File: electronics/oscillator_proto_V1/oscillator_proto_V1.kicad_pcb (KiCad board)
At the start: 2 copper layers, 42.5 x 46.2 mm, 27 parts, among them J1 module_2x15_left_input, J2 module_2x15_right_input, J3 Coax, U1 TL081, U2 LME49720, U3 TL082

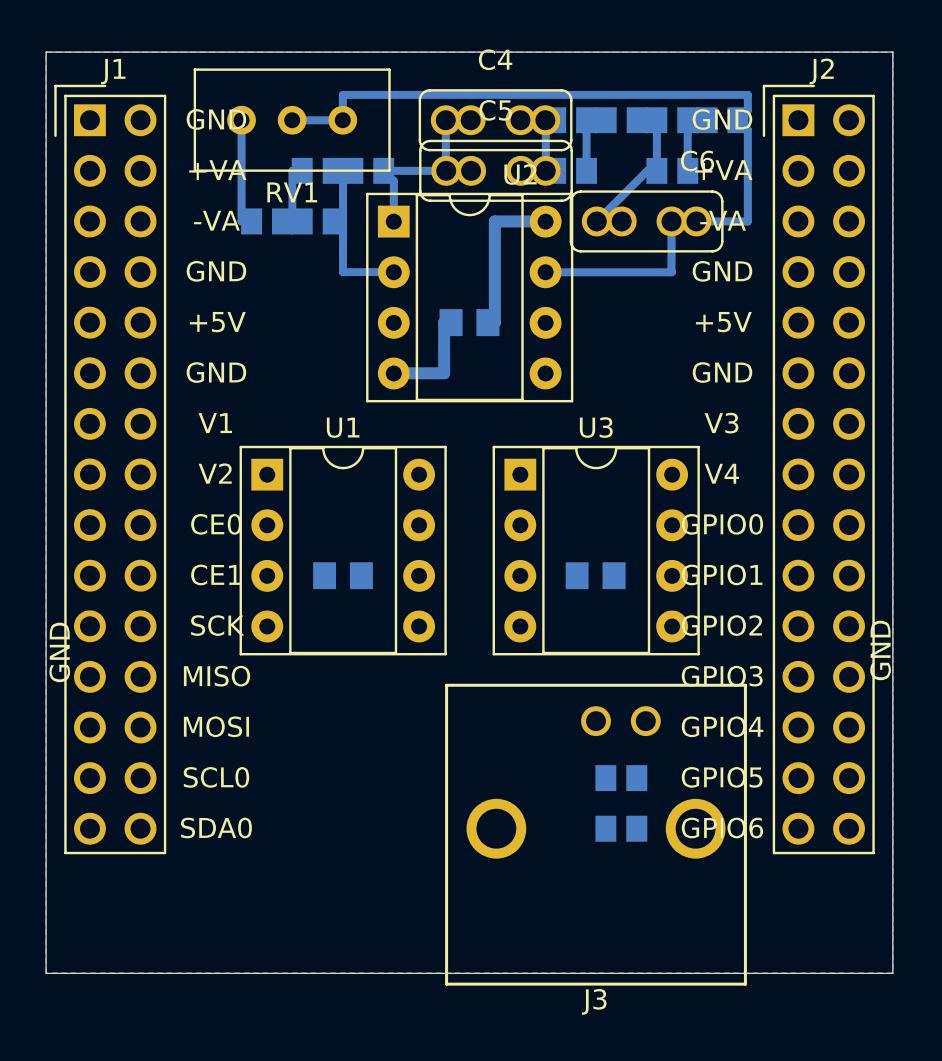
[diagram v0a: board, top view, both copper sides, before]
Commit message: layout completed on prototype oscillator prototype
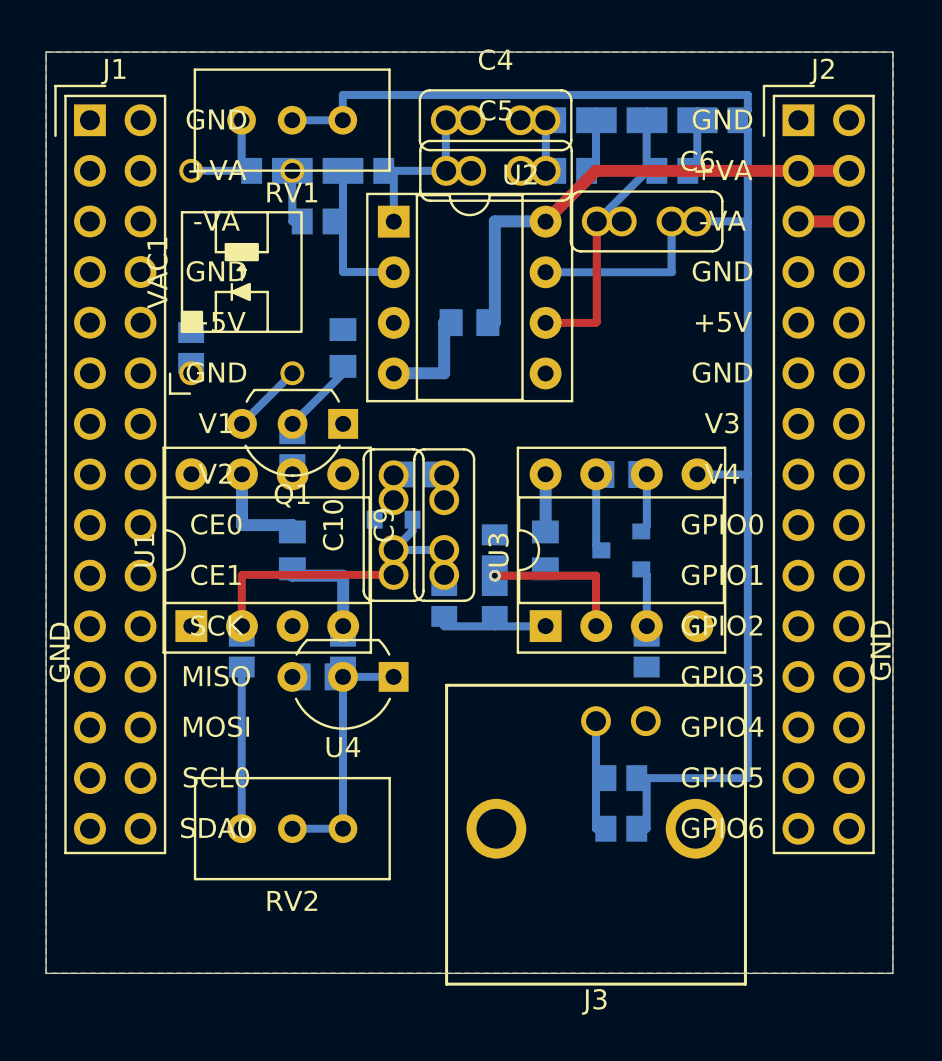
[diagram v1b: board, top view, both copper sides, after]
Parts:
- added C10: 100n, SquantorRcl:C-025_050-030X100-film, F.Cu at (160.0, 92.7)
- added C11: 10u, SquantorRcl:C_0805+0603, B.Cu at (157.5, 83.8)
- added C7: 47p, SquantorRcl:C_0805+0603, B.Cu at (171.4, 90.2)
- added C8: 10u, SquantorRcl:C_0805+0603, B.Cu at (156.2, 100.3)
- added C9: 47u, SquantorRcl:C-025_050-030X100-film, F.Cu at (162.6, 92.7)
- added D1: BAV99, SquantorIC:SOT23-3, B.Cu at (171.4, 94.0)
- added D2: BAV99, SquantorIC:SOT23-3, B.Cu at (160.0, 91.4)
- added Q1: BC337, Package_TO_SOT_THT:TO-92L_Inline_Wide, F.Cu at (157.5, 87.6)
- added R13: 510, SquantorRcl:R_0805+0603, B.Cu at (149.9, 83.8)
- added R14: 10K, SquantorRcl:R_0805+0603, B.Cu at (165.1, 96.5)
- added R15: 10K, SquantorRcl:R_0805+0603, B.Cu at (165.1, 94.0)
- added R16: 10K, SquantorRcl:R_0805+0603, B.Cu at (172.7, 99.1)
- added R17: 8K2, SquantorRcl:R_0805+0603, B.Cu at (157.5, 99.1)
- added R18: 27K, SquantorRcl:R_0805+0603, B.Cu at (162.6, 96.5)
- added R19: 8K2, SquantorRcl:R_0805+0603, B.Cu at (152.4, 99.1)
- added R20: 8K2, SquantorRcl:R_0805+0603, B.Cu at (161.3, 90.2)
- added R21: 2K2, SquantorRcl:R_0805+0603, B.Cu at (154.9, 88.9)
- added RV2: 50K, Potentiometer_THT:Potentiometer_Bourns_3296W_Vertical, F.Cu at (152.4, 108.0)
- added U4: TL431, Package_TO_SOT_THT:TO-92_Inline_Wide, F.Cu at (160.0, 100.3)
- added VAC1: NSL32R3, SquantorOpto:NSL32SR3, F.Cu at (152.4, 80.0)
- moved N1 8.98 mm to (165.7, 105.5)
- moved N2 8.98 mm to (165.1, 101.6)
- moved U1 8.50 mm to (149.9, 97.8), turned to 90 degrees
- moved U3 7.71 mm to (167.7, 97.8), turned to 90 degrees
- moved C1 2.84 mm to (154.9, 94.0), turned to 90 degrees
- moved C3 2.82 mm to (167.6, 94.0), turned to 90 degrees
- moved R9 2.54 mm to (153.7, 74.9)
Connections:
- U1 pad 2: unconnected-(U1-Pad2) -> Net-(U1-Pad2)
- U1 pad 3: unconnected-(U1-Pad3) -> GND
- U1 pad 6: unconnected-(U1-Pad6) -> Net-(U1-Pad6)
- U3 pad 1: unconnected-(U3-Pad1) -> /GAIN_INPUT
- U3 pad 2: unconnected-(U3-Pad2) -> Net-(U3-Pad2)
- U3 pad 3: unconnected-(U3-Pad3) -> Net-(R16-Pad2)
- U3 pad 5: unconnected-(U3-Pad5) -> /OUTPUT
- U3 pad 6: unconnected-(U3-Pad6) -> Net-(U3-Pad6)
- U3 pad 7: unconnected-(U3-Pad7) -> Net-(U3-Pad7)
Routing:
- net /OUTPUT: track 42.4 -> 81.5 mm
- net +15V: track 7.98 -> 32.6 mm
- net Net-(U1-Pad2): track 0.00 -> 14.6 mm
- net Net-(C8-Pad2): track 0.00 -> 12.7 mm
- net Net-(U2-Pad6): track 7.60 -> 16.0 mm
- net Net-(R19-Pad2): track 0.00 -> 8.12 mm
- net -15V: track 5.42 -> 13.4 mm
- net Net-(U3-Pad2): track 0.00 -> 7.61 mm, vias 0 -> 1
- net Net-(J3-Pad1): track 0.00 -> 6.39 mm
- net /GAIN_INPUT: track 0.00 -> 6.08 mm
- net Net-(C11-Pad2): track 0.00 -> 3.93 mm
- net Net-(U3-Pad7): track 0.00 -> 3.93 mm
- net /GAIN: track 0.00 -> 3.59 mm
- net Net-(U3-Pad6): track 0.00 -> 2.99 mm
- net Net-(R16-Pad2): track 0.00 -> 2.97 mm
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
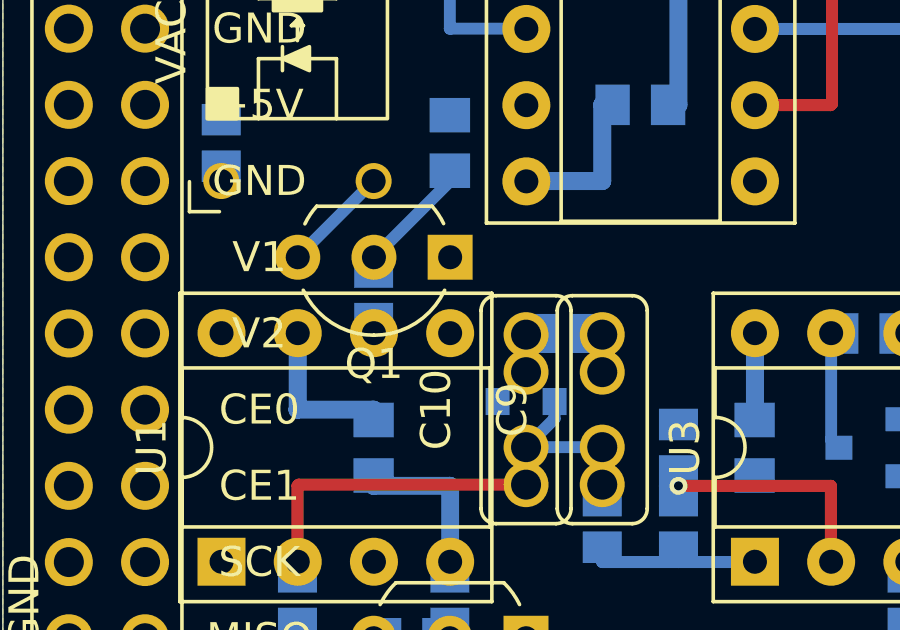
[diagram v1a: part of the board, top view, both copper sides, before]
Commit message: updated resistor values and some minor routing updates
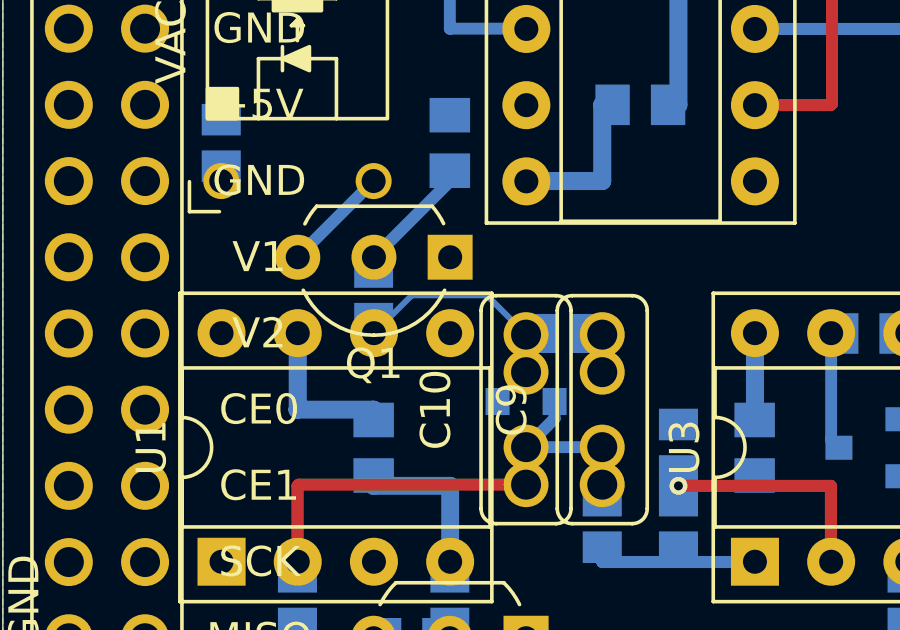
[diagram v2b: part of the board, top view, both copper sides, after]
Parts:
- N1: value 20220421 -> 20220423
- R11, R12: value 3k6 -> 3k
- R9: value 18 -> 15
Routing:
- net Net-(C10-Pad2): track 0.00 -> 6.13 mm

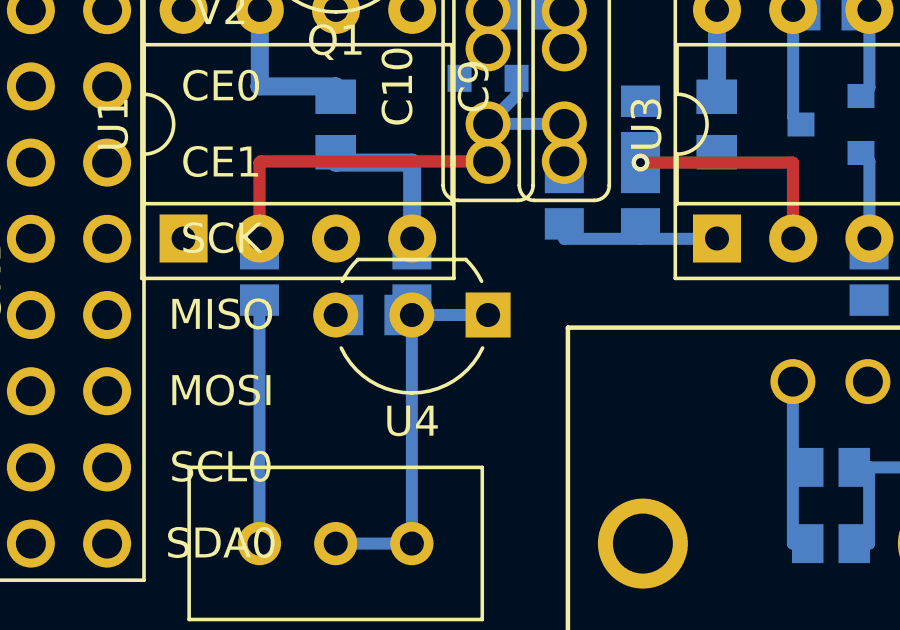
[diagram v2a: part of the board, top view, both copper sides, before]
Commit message: fixed errors with proto oscillator
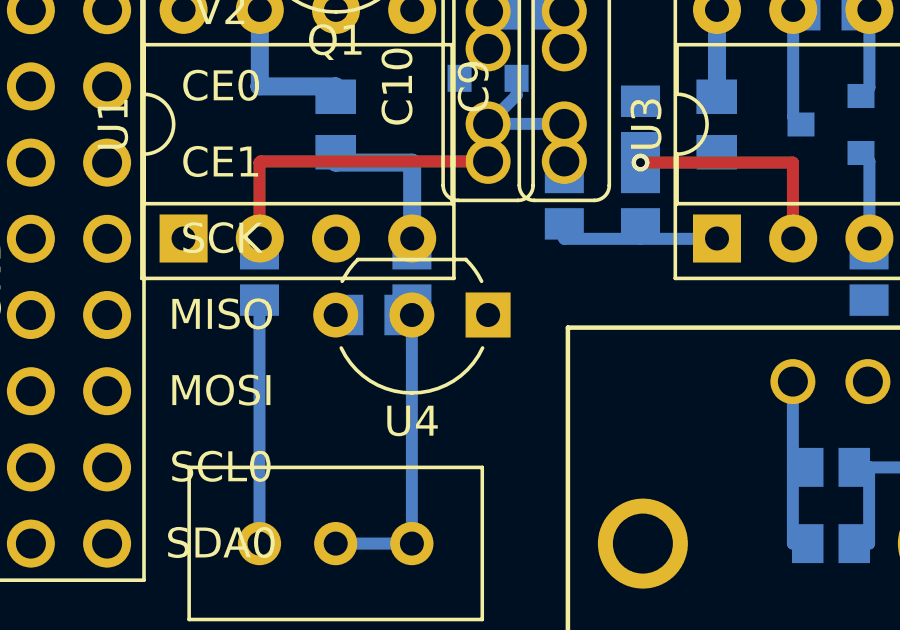
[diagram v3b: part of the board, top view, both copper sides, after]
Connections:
- U4 pad 1: Net-(C8-Pad2) -> GND
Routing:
- net Net-(C8-Pad2): track 12.7 -> 10.2 mm
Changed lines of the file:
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@@
     (fp_arc (start 0.786375 1.753625) (mid 0.248779 -0.949055) (end 2.54 -2.48) (layer "F.Fab") (width 0.1))
     (pad "1" thru_hole rect (at 0 0 180) (size 1.5 1.5) (drill 0.8) (layers *.Cu *.Mask)
-      (net 43 "Net-(C8-Pad2)") (pinfunction "REF") (pintype "passive"))
+      (net 1 "GND") (pinfunction "REF") (pintype "passive"))
     (pad "2" thru_hole circle (at 2.54 0 180) (size 1.5 1.5) (drill 0.8) (layers *.Cu *.Mask)
       (net 43 "Net-(C8-Pad2)") (pinfunction "A") (pintype "passive"))
@@
   (segment (start 152.41 87.62) (end 154.94 85.09) (width 0.4) (layer "B.Cu") (net 42))
   (segment (start 157.48 107.95) (end 157.48 100.33) (width 0.4) (layer "B.Cu") (net 43))
-  (segment (start 157.48 100.33) (end 160.02 100.33) (width 0.4) (layer "B.Cu") (net 43))
   (segment (start 154.94 107.95) (end 157.48 107.95) (width 0.4) (layer "B.Cu") (net 43))
   (segment (start 158.71 88.9) (end 156.21 88.9) (width 0.2) (layer "B.Cu") (net 44))

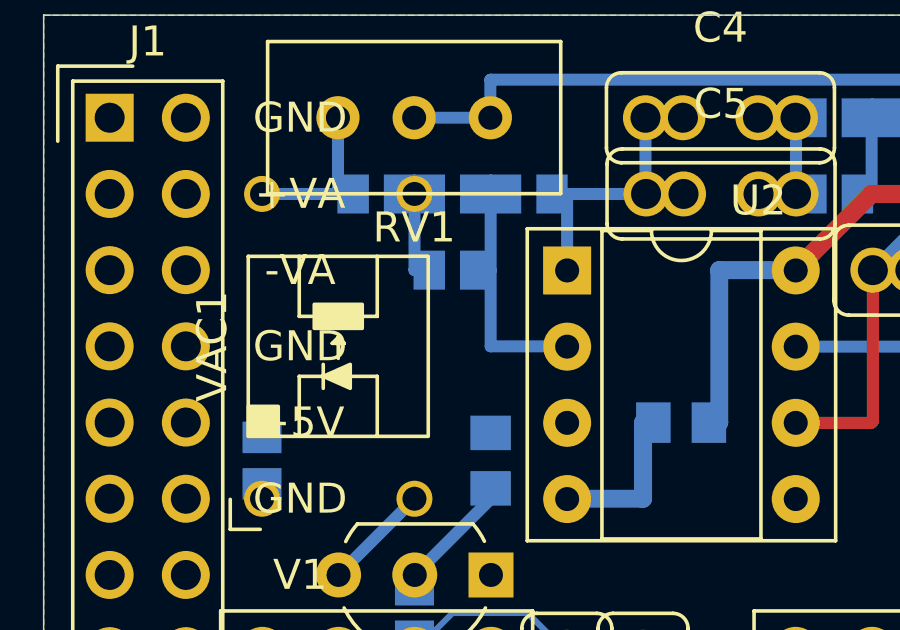
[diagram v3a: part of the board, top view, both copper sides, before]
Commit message: added additional adjust resistor and updated values
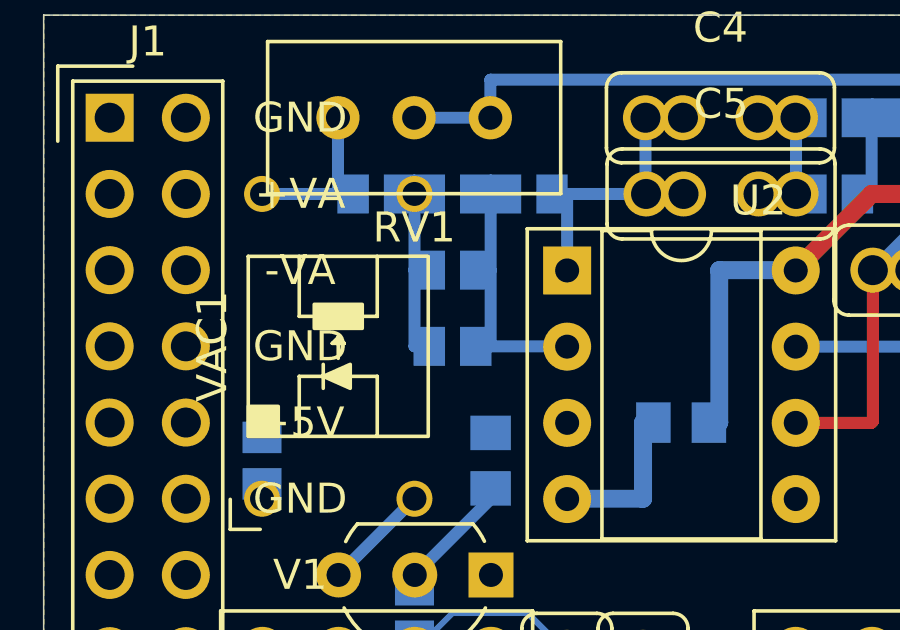
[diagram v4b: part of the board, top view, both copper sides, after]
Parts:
- added R22: ADJ, SquantorRcl:R_0805+0603, B.Cu at (156.2, 80.0)
- N1: value 20220423 -> 20220428
- R11, R12: value 3k -> 3K6
- R9: value 15 -> 18
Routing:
- net Net-(R10-Pad1): track 3.03 -> 6.07 mm
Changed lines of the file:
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@@
       (effects (font (size 1 1) (thickness 0.15)) (justify mirror))
     )
-    (fp_text value "20220423" (at 0.8 0.1) (layer "B.SilkS")
+    (fp_text value "20220428" (at 0.8 0.1) (layer "B.SilkS")
       (effects (font (size 0.8 0.8) (thickness 0.15)) (justify mirror))
     )
@@
   )
   (footprint "SquantorRcl:R_0805+0603" (layer "B.Cu")
+    (at 156.21 80.01)
+    (descr "Resistor SMD 0805, reflow soldering, Vishay (see dcrcw.pdf)")
+    (tags "resistor 0805")
+    (property "Sheetfile" "oscillator_proto_V1.kicad_sch")
+    (property "Sheetname" "")
+    (attr smd)
+    (fp_text reference "R22" (at 0 2.1) (layer "B.SilkS")
+      (effects (font (size 1 1) (thickness 0.15)) (justify mirror))
+    )
+    (fp_text value "ADJ" (at 0 -2.1) (layer "B.Fab")
+      (effects (font (size 1 1) (thickness 0.15)) (justify mirror))
+    )
+    (fp_poly (pts
+        (xy -0.1 0.6)
+        (xy -0.1 -0.6)
+        (xy 0.1 -0.6)
+        (xy 0.1 0.6)
+      ) (layer "B.SilkS") (width 0.1) (fill solid))
+    (fp_line (start -1.55 0.95) (end -1.55 -0.95) (layer "B.CrtYd") (width 0.05))
+    (fp_line (start -1.55 -0.95) (end 1.55 -0.95) (layer "B.CrtYd") (width 0.05))
+    (fp_line (start -1.55 0.95) (end 1.55 0.95) (layer "B.CrtYd") (width 0.05))
+    (fp_line (start 1.55 0.95) (end 1.55 -0.95) (layer "B.CrtYd") (width 0.05))
+    (fp_line (start -1 0.625) (end 1 0.625) (layer "B.Fab") (width 0.1))
+    (fp_line (start -1 -0.625) (end -1 0.625) (layer "B.Fab") (width 0.1))
+    (fp_line (start 1 -0.625) (end -1 -0.625) (layer "B.Fab") (width 0.1))
+    (fp_line (start 1 0.625) (end 1 -0.625) (layer "B.Fab") (width 0.1))
+    (pad "1" smd rect (at -0.775 0) (size 1.05 1.3) (layers "B.Cu" "B.Paste" "B.Mask")
+      (net 37 "Net-(R10-Pad1)") (pintype "passive"))
+    (pad "2" smd rect (at 0.775 0) (size 1.05 1.3) (layers "B.Cu" "B.Paste" "B.Mask")
+      (net 51 "Net-(R10-Pad2)") (pintype "passive"))
+    (model "${KICAD6_3DMODEL_DIR}/Resistor_SMD.3dshapes/R_0805_2012Metric.step"
+      (offset (xyz 0 0 0))
+      (scale (xyz 1 1 1))
+      (rotate (xyz 0 0 0))
+    )
+  )
+  (footprint "SquantorRcl:R_0805+0603" (layer "B.Cu")
     (at 165.1 96.52 90)
     (descr "Resistor SMD 0805, reflow soldering, Vishay (see dcrcw.pdf)")
@@
       (effects (font (size 1 1) (thickness 0.15)) (justify mirror))
     )
-    (fp_text value "15" (at 0 -2.1) (layer "B.Fab")
+    (fp_text value "18" (at 0 -2.1) (layer "B.Fab")
       (effects (font (size 1 1) (thickness 0.15)) (justify mirror))
     )
@@
       (effects (font (size 1 1) (thickness 0.15)) (justify mirror))
     )
-    (fp_text value "3k" (at 0 -2.1) (layer "B.Fab")
+    (fp_text value "3K6" (at 0 -2.1) (layer "B.Fab")
       (effects (font (size 1 1) (thickness 0.15)) (justify mirror))
     )
@@
       (effects (font (size 1 1) (thickness 0.15)) (justify mirror))
     )
-    (fp_text value "3k" (at 0 -2.1) (layer "B.Fab")
+    (fp_text value "3K6" (at 0 -2.1) (layer "B.Fab")
       (effects (font (size 1 1) (thickness 0.15)) (justify mirror))
     )
@@
   (segment (start 152.39 74.92) (end 152.4 74.93) (width 0.4) (layer "B.Cu") (net 36))
   (segment (start 152.39 72.39) (end 152.39 74.92) (width 0.4) (layer "B.Cu") (net 36))
+  (segment (start 155.435 80.01) (end 154.94 80.01) (width 0.4) (layer "B.Cu") (net 37))
   (segment (start 154.94 77.47) (end 154.94 74.93) (width 0.4) (layer "B.Cu") (net 37))
-  (segment (start 155.435 77.47) (end 154.94 77.47) (width 0.4) (layer "B.Cu") (net 37))
+  (segment (start 154.94 80.01) (end 154.94 77.47) (width 0.4) (layer "B.Cu") (net 37))
+  (segment (start 154.94 77.47) (end 155.435 77.47) (width 0.4) (layer "B.Cu") (net 37))
   (segment (start 170.19 90.16) (end 170.19 93.72) (width 0.4) (layer "B.Cu") (net 38))
   (segment (start 170.19 93.72) (end 170.45 93.98) (width 0.4) (layer "B.Cu") (net 38))
